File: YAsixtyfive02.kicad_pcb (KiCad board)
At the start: 2 copper layers, 99.7 x 99.7 mm, 60 parts, among them J1 ~{NMI}, J2 Aux 5VDC, J3 Power 5V, J4 Expansion Bus, J7 GND, J8 FTDI Serial2USB, SW1 RESET, SW2 SW_Push_DPDT, U1 WD65C02, U10 74LS138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

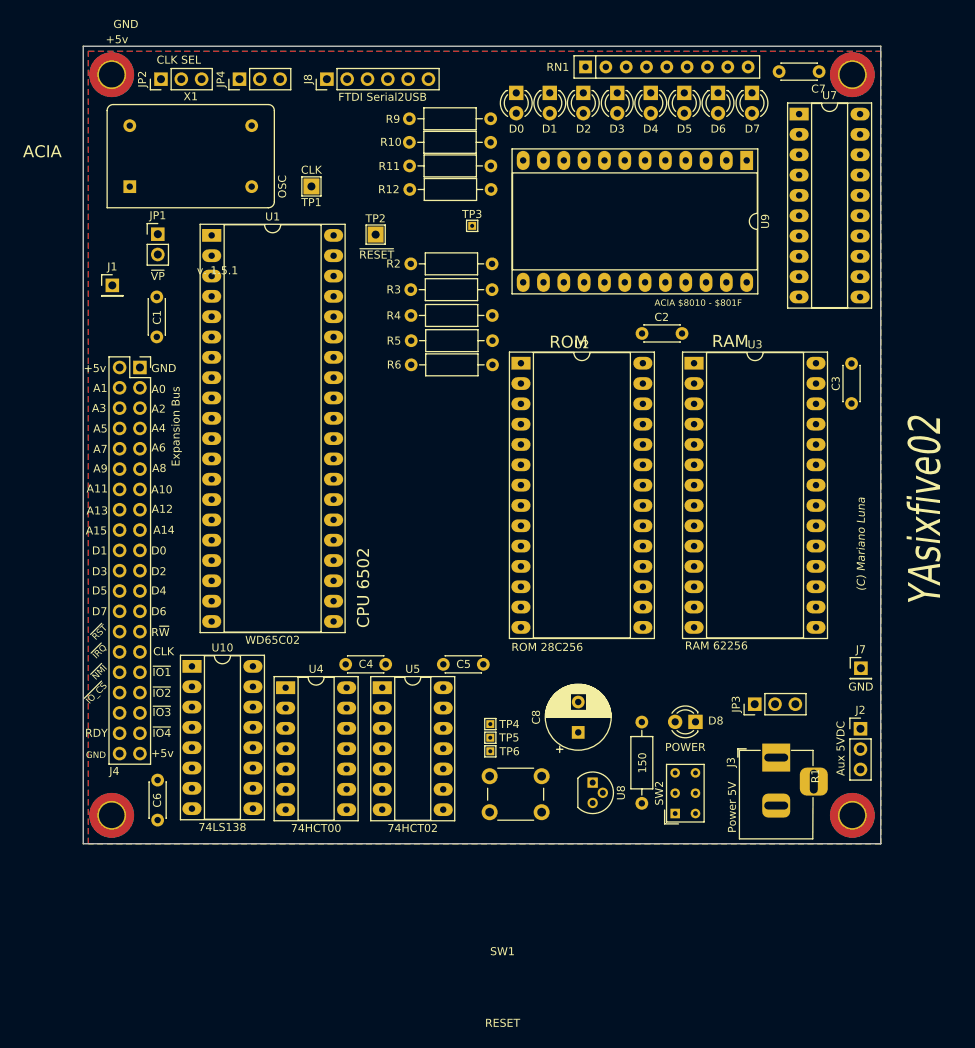
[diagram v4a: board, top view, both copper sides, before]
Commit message: PCB Almost ready missing USB Power override
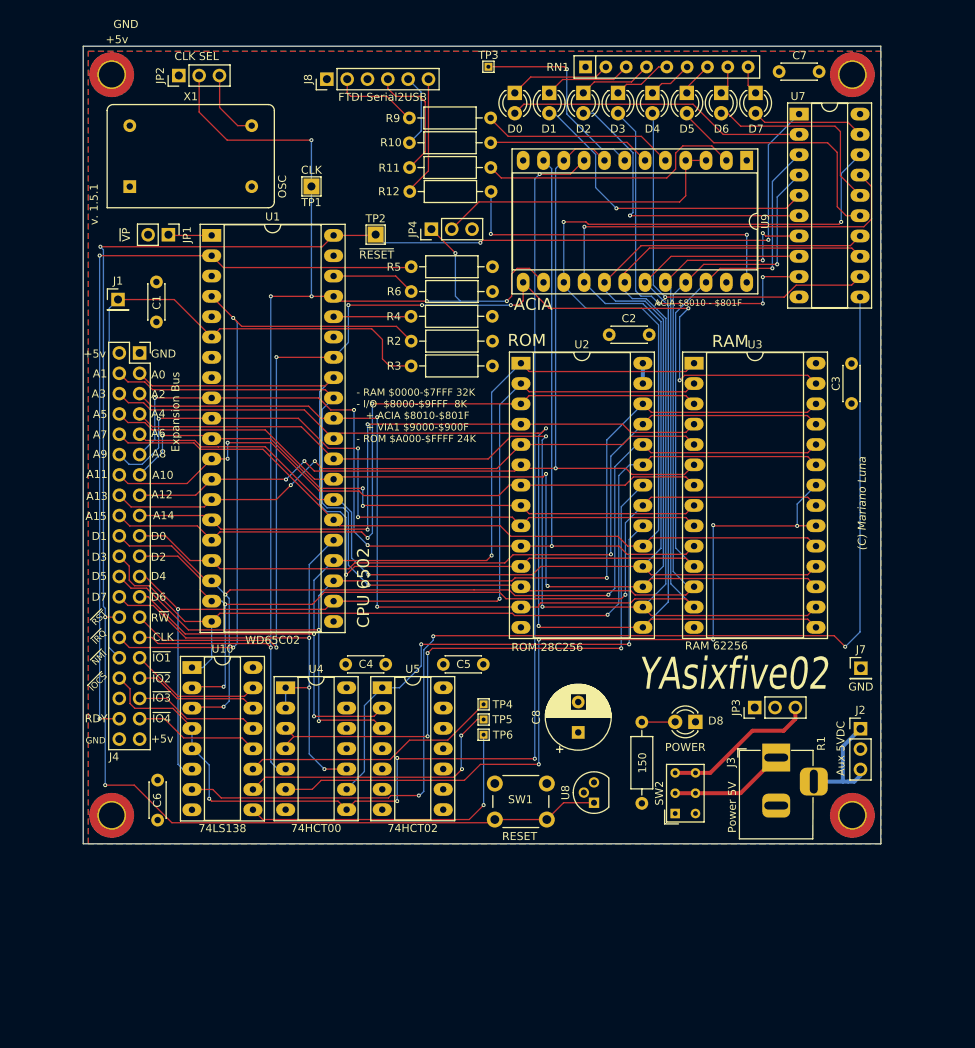
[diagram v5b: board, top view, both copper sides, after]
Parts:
- moved JP4 30.4 mm to (74.6, 73.0)
- moved TP3 20.0 mm to (81.8, 52.7)
- moved R2 9.66 mm to (82.3, 87.0)
- moved R3 9.54 mm to (82.3, 90.1)
- moved R5 9.24 mm to (82.3, 77.7)
- moved R6 9.16 mm to (72.1, 80.8)
- moved SW1 6.86 mm to (82.6, 142.3), turned to 0 degrees
- moved C2 4.11 mm to (101.9, 86.2)
- moved TP4 2.61 mm to (81.2, 132.4)
- moved U8 2.52 mm to (95.0, 144.7), turned to 90 degrees
- moved TP5 2.42 mm to (81.2, 134.3)
- moved JP2 2.27 mm to (43.1, 53.8)
- moved TP6 2.24 mm to (81.2, 136.2)
- moved J1 1.91 mm to (35.5, 81.8)
- moved C1 1.87 mm to (40.3, 84.6)
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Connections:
- net Net-(J8-Pad2) renamed /CTS
- net Net-(J8-Pad4) renamed /TX
- net Net-(J8-Pad5) renamed /RX
- net Net-(J8-Pad6) renamed /RTS
- J4 pad 10: a7 -> d7
- J4 pad 11: a8 -> a0
- J4 pad 12: a9 -> a1
- J4 pad 13: a10 -> a2
- J4 pad 14: a11 -> a3
- J4 pad 15: a12 -> a4
- J4 pad 16: a13 -> a5
- J4 pad 17: a14 -> a6
- J4 pad 18: a15 -> a7
- J4 pad 19: d0 -> a8
- J4 pad 20: d1 -> a9
- J4 pad 21: d2 -> a10
- J4 pad 22: d3 -> a11
- J4 pad 23: d4 -> a12
- J4 pad 24: d5 -> a13
- J4 pad 25: d6 -> a14
- J4 pad 26: d7 -> a15
- J4 pad 3: a0 -> d0
- J4 pad 4: a1 -> d1
- J4 pad 5: a2 -> d2
- J4 pad 6: a3 -> d3
- J4 pad 7: a4 -> d4
- J4 pad 8: a5 -> d5
- J4 pad 9: a6 -> d6
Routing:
- net ~{RESET}: track 0.00 -> 235.4 mm, vias 0 -> 5
- net d6: track 0.00 -> 189.0 mm, vias 0 -> 2
- net d7: track 0.00 -> 188.4 mm, vias 0 -> 2
- net d4: track 0.00 -> 188.1 mm, vias 0 -> 2
- net d5: track 0.00 -> 184.2 mm, vias 0 -> 2
- net d3: track 0.00 -> 183.1 mm, vias 0 -> 2
- net CLK: track 0.00 -> 165.8 mm, vias 0 -> 7
- net d1: track 0.00 -> 162.2 mm, vias 0 -> 2
- net d0: track 0.00 -> 160.4 mm, vias 0 -> 2
- net d2: track 0.00 -> 158.8 mm, vias 0 -> 4
- net ~{IO_CS}: track 0.00 -> 149.4 mm, vias 0 -> 5
- net ~{IO_8}: track 0.00 -> 146.2 mm, vias 0 -> 3
- net R~{W}: track 0.00 -> 143.0 mm, vias 0 -> 7
- net a0: track 0.00 -> 141.3 mm, vias 0 -> 4
- net a13: track 0.00 -> 134.9 mm, vias 0 -> 3
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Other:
- board text added: "~{IOCS}"
- board text removed: "~{IO_CS}"

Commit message: PCB Completed CPU/ACIA/RAM/ROM
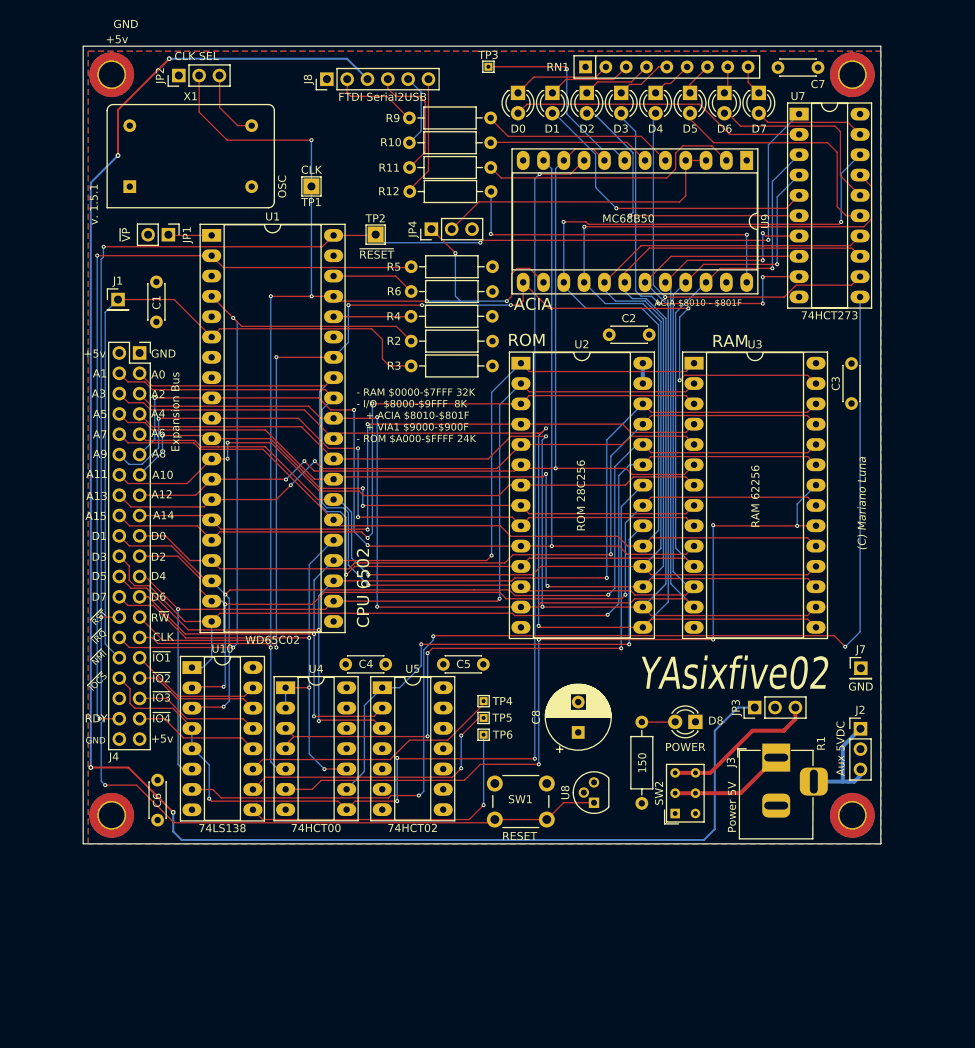
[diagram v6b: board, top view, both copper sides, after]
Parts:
- U9: value MC6850_ -> MC68B50
- moved C7 0.53 mm to (123.0, 52.8)
- moved D2 0.44 mm to (94.1, 56.0)
- moved D0 0.40 mm to (85.5, 56.0)
- moved D1 0.40 mm to (89.8, 56.0)
- moved D4 0.40 mm to (102.7, 56.0)
- moved D5 0.40 mm to (107.0, 56.0)
- moved D6 0.40 mm to (111.3, 56.0)
- moved TP4 0.40 mm to (81.2, 132.0)
- moved D3 0.40 mm to (98.4, 56.0)
- moved D7 0.40 mm to (115.6, 56.0)
- moved TP5 0.20 mm to (81.2, 134.1)
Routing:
- net USB_5V: track 0.00 -> 220.7 mm, vias 0 -> 4

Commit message: rev 1.6.0 ready new memory map
CPU/ROM/RAM/ACIA/SR New memory map, io in expansion port
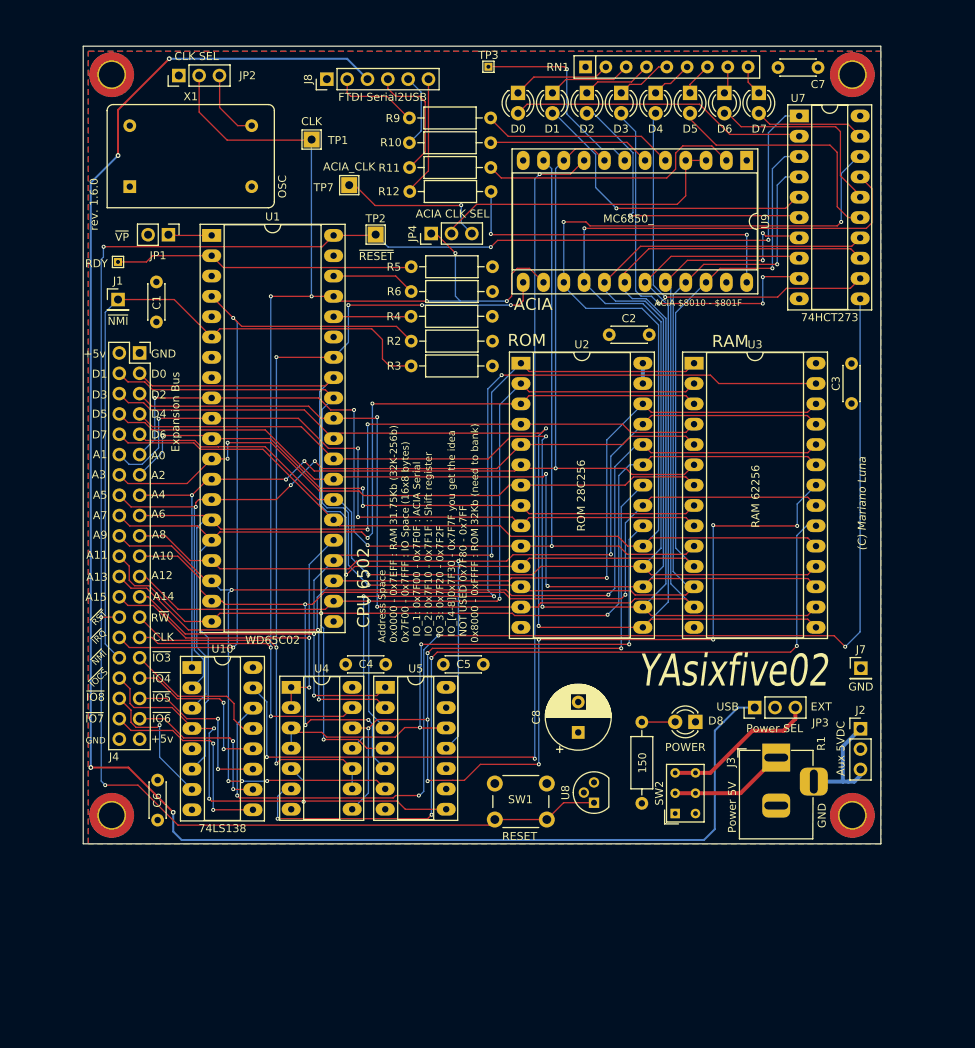
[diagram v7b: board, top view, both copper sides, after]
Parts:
- removed TP5: IO6, TestPoint:TestPoint_THTPad_1.0x1.0mm_Drill0.5mm
- removed TP6: IO7, TestPoint:TestPoint_THTPad_1.0x1.0mm_Drill0.5mm
- added TP7: ACIA_CLK, TestPoint:TestPoint_THTPad_2.0x2.0mm_Drill1.0mm, F.Cu at (64.4, 67.5)
- JP3: value Aux 5VDC -> Power SEL
- TP4: value IO5 -> RDY
- U5: value 74HCT02 -> 74LS30
- U9: value MC68B50 -> MC6850_
- moved TP4 71.4 mm to (35.5, 77.1)
- moved TP1 5.86 mm to (59.7, 61.8)
- moved U4 0.70 mm to (57.1, 130.3)
- moved JP4 0.55 mm to (74.6, 73.6)
- moved U5 0.37 mm to (68.9, 130.3)
- moved U7 0.23 mm to (120.6, 58.9)
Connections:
- J4 pad 31: ~{IO_1} -> ~{IO_3}
- J4 pad 33: ~{IO_2} -> ~{IO_4}
- J4 pad 35: ~{IO_3} -> ~{IO_5}
- J4 pad 36: unconnected-(J4-Pad36) -> ~{IO_8}
- J4 pad 37: ~{IO_4} -> ~{IO_6}
- J4 pad 38: RDY -> ~{IO_7}
- TP4 pad 1: ~{IO_5} -> RDY
- U10 pad 1: a11 -> a4
- U10 pad 2: a10 -> a5
- U10 pad 3: a9 -> a6
- U10 pad 5: ~{IO_CS} -> +5V
- U10 pad 6: a12 -> a7
- U2 pad 22: ~{ROM_OE} -> ~{RD}
- U3 pad 22: ~{RAM_CS} -> ~{RD}
- U3 pad 27: R~{W} -> ~{WR}
- U4 pad 10: a15 -> R~{W}
- U4 pad 11: unconnected-(U4-Pad11) -> ~{WR}
- U4 pad 12: GND -> ~{RD}
- U4 pad 13: GND -> CLK
- U4 pad 3: ~{ROM_OE} -> ~{ROM_CS}
- U4 pad 4: ~{ROM_OE} -> ~{ROM_CS}
- U4 pad 5: CLK -> ~{IO_CS}
- U4 pad 8: ~{IO_CS} -> ~{RD}
- U4 pad 9: ~{ROM_CS} -> R~{W}
- U5 pad 1: ~{ROM_CS} -> a14
- U5 pad 10: unconnected-(U5-Pad10) -> (no net)
- U5 pad 11: GND -> a8
- U5 pad 12: GND -> ~{ROM_CS}
- U5 pad 13: unconnected-(U5-Pad13) -> (no net)
- U5 pad 2: a14 -> a13
- U5 pad 3: a13 -> a12
- U5 pad 4: unconnected-(U5-Pad4) -> a11
- U5 pad 5: GND -> a10
- U5 pad 6: GND -> a9
- U5 pad 8: GND -> ~{IO_CS}
- U5 pad 9: GND -> (no net)
- U7 pad 11: ~{IO_8} -> ~{IO_2}
- U9 pad 9: ~{IO_CS} -> ~{IO_1}
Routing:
- net ~{RD}: track 0.00 -> 165.9 mm, vias 0 -> 10
- net ~{IO_2}: track 15.7 -> 151.5 mm, vias 0 -> 4
- net ~{IO_8}: track 146.2 -> 17.3 mm, vias 3 -> 1
- net ~{IO_1}: track 16.6 -> 122.6 mm, vias 0 -> 3
- net ~{WR}: track 0.00 -> 104.3 mm, vias 0 -> 3
- net ~{IO_CS}: track 149.4 -> 59.7 mm, vias 5 -> 3
- net ~{ROM_OE}: track 76.5 -> 0.00 mm, vias 3 -> 0
- net RDY: track 100.4 -> 37.6 mm, vias 2 -> 0
- net a7: track 91.2 -> 121.6 mm
- net a6: track 84.0 -> 110.0 mm
- net a9: track 126.8 -> 151.9 mm, vias 3 -> 5
- net a5: track 77.3 -> 101.4 mm, vias 2 -> 3
- net a8: track 101.8 -> 125.9 mm, vias 1 -> 2
- net R~{W}: track 143.0 -> 121.0 mm, vias 7 -> 6
- net a4: track 118.1 -> 139.7 mm, vias 3 -> 4
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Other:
- board text added: "+ JP1: ~{VP} Closed NMOS | Open CMOS + JP2: Clock Selector 1. GND | 2. CLK IN | 3. OSC OUT + JP3: Power Selector Jumper 1-2 USB | 2-3 Jack + JP4: ACIA Clock (TP7) 1. CLK | 2. TX CLK IN | 3. TX_EXT + J1: ~{NMI} IN + J2: Aux Power In (switched) 1. GND | 2. 5v IN | 3. GND"
- board text added: "Address Space 0x0000 - 0x7EFF : RAM 31.75Kb (32K-256b) 0x7F00 - 0x7FFF : IO Space (16x8 bytes) IO_1: 0x7F00 - 0x7F0F : ACIA Serial IO_2: 0x7F10 - 0x7F1F : Shift register IO_3: 0x7F20 - 0x7F2F IO_[4-8]0x7F30 - 0x7F7F you get the idea NOT USED 0x7F80 - 0x7FF 0x8000 - 0xFFFF : ROM 32Kb (need to bank)"
- board text added: "EXT"
- board text added: "USB"
- board text added: "rev. 1.6.0"
- board text added: "~{IO5}"
- board text added: "~{IO6}"
- board text added: "~{IO7}"
- board text added: "~{IO8}"
- board text removed: "+ JP1: Closed NMOS | Open CMOS + JP2: 1. GND | 2. PHI2 IN | 3. OSC OUT + JP3: Power via USB + J1: ~{NMI} IN"
- board text removed: "- RAM $0000-$7FFF 32K - I/O $8000-$9FFF 8K + ACIA $8010-$801F + VIA1 $9000-$900F - ROM $A000-$FFFF 24K"
- board text removed: "RDY"
- board text removed: "v. 1.5.1"
- board text removed: "~{IO1}"
- board text removed: "~{IO2}"

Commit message: Clean up and minor PCB tweaks
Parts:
- TP3: value IO7 -> ACIA IRQ
- moved RN1 0.74 mm to (93.2, 52.8)
- moved C7 0.60 mm to (122.4, 52.8)
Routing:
- net ~{RESET}: track 237.1 -> 238.9 mm
- net Net-(D2-Pad1): track 8.81 -> 8.06 mm
- net Net-(D0-Pad1): track 12.3 -> 11.6 mm
- net Net-(D3-Pad1): track 7.05 -> 6.30 mm
- net Net-(D1-Pad1): track 10.6 -> 9.82 mm
- net Net-(D4-Pad1): track 5.29 -> 4.57 mm
